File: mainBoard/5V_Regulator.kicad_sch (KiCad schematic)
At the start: 18 parts, among them IC1 LT8631IFE#PBF

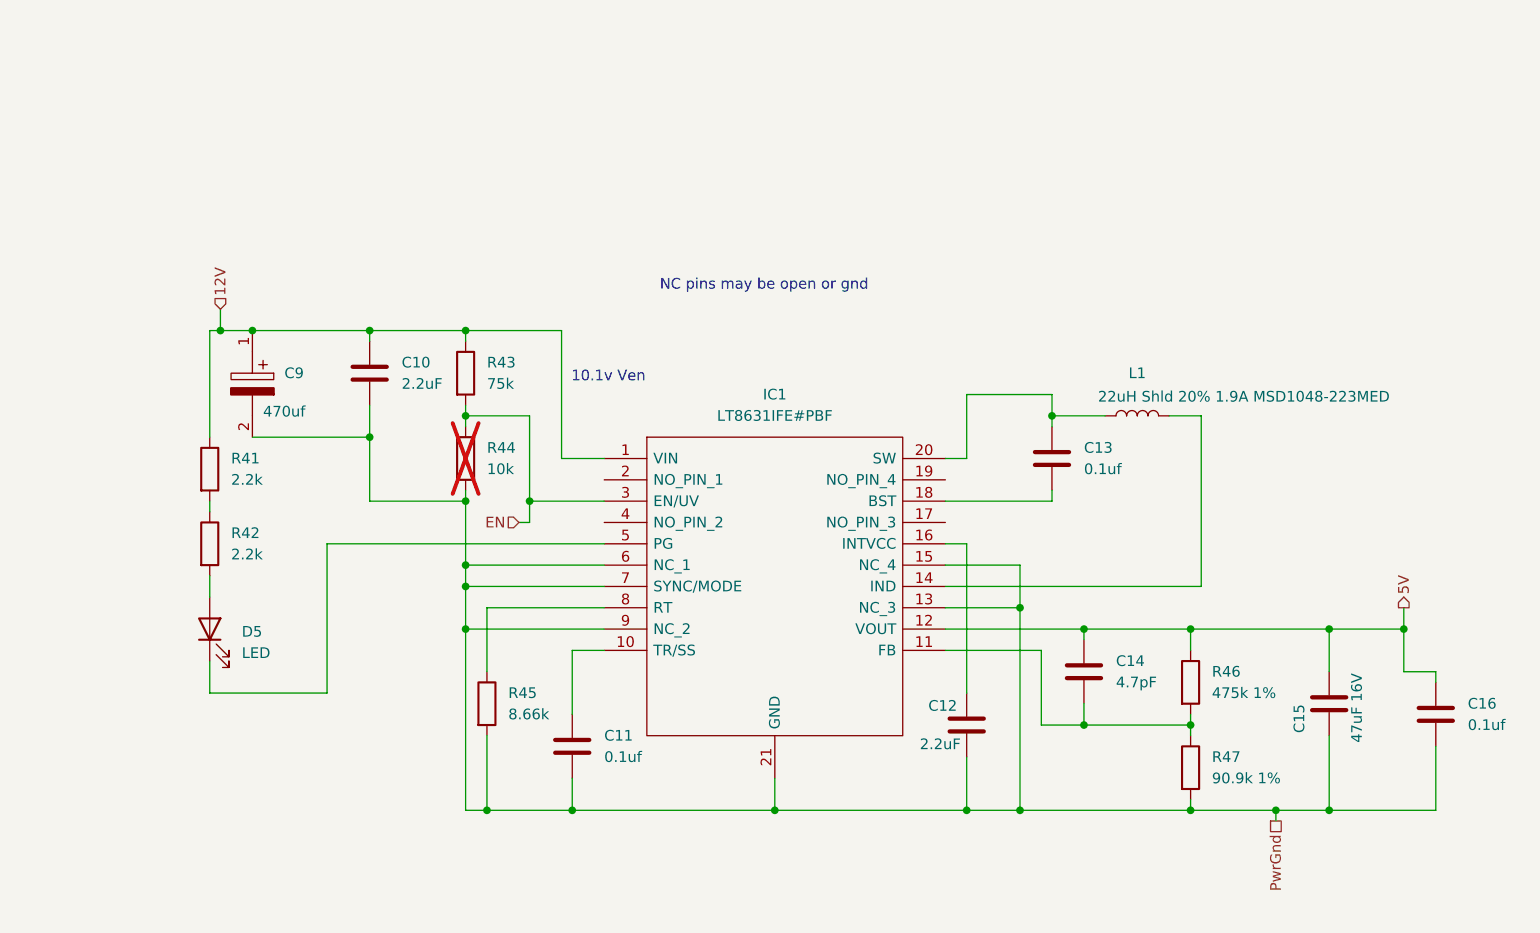
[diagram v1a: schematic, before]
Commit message: need to finish new regulators and run parts check on sch
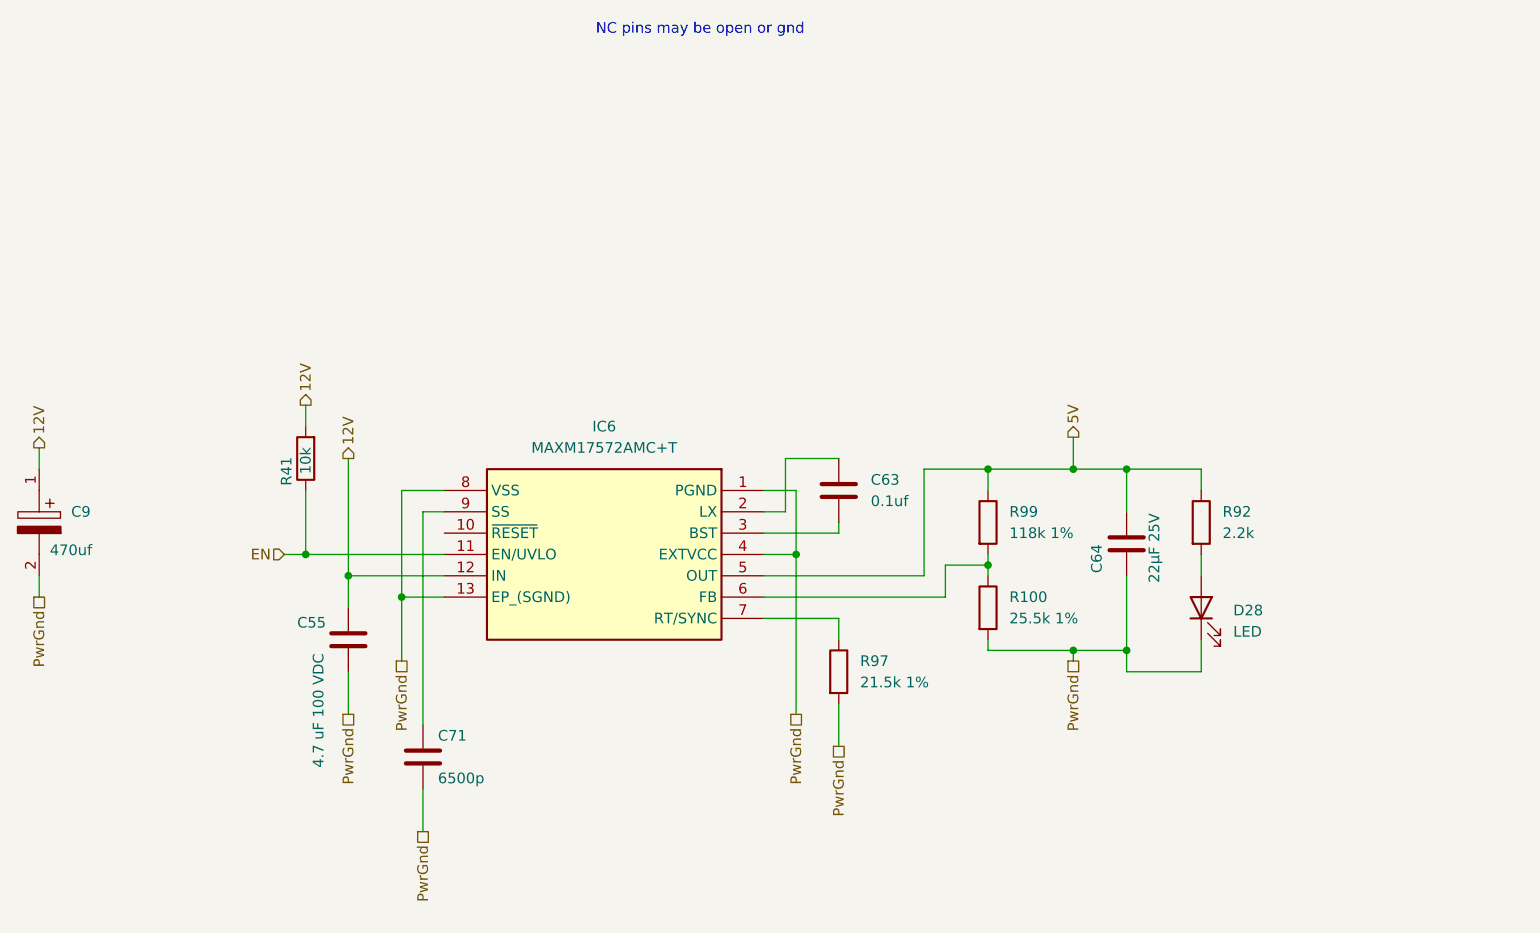
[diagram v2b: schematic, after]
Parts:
- removed C10, C12: 2.2uF, Capacitor_SMD:C_1206_3216Metric, symbol Device:C
- removed C11, C13, C16: 0.1uf, Capacitor_SMD:C_0402_1005Metric, symbol Device:C
- removed C14: 4.7pF, Capacitor_SMD:C_0402_1005Metric, symbol Device:C
- removed C15: 47uF 16V, Capacitor_SMD:C_1210_3225Metric, symbol Device:C
- removed D5: LED, LED_SMD:LED_0402_1005Metric, symbol Device:LED
- removed IC1: LT8631IFE#PBF, SamacSys_Parts:SOP65P640X120-21N, symbol SamacSys_Parts:LT8631IFE#PBF
- removed L1: 22uH Shld 20% 1.9A MSD1048-223MED, Inductor_SMD:L_Bourns_SRP1038C_10.0x10.0mm, symbol Device:L
- removed R42: 2.2k, Resistor_SMD:R_0805_2012Metric, symbol Device:R
- removed R43: 75k, Resistor_SMD:R_0402_1005Metric, symbol Device:R
- removed R44: 10k, Resistor_SMD:R_0402_1005Metric, symbol Device:R
- removed R45: 8.66k, Resistor_SMD:R_0402_1005Metric, symbol Device:R
- removed R46: 475k 1%, Resistor_SMD:R_0402_1005Metric, symbol Device:R
- removed R47: 90.9k 1%, Resistor_SMD:R_0402_1005Metric, symbol Device:R
- added C55: 4.7 uF 100 VDC, Capacitor_SMD:C_1206_3216Metric, symbol Device:C
- added C63: 0.1uf, Capacitor_SMD:C_0402_1005Metric, symbol Device:C
- added C64: 22μF 25V, Capacitor_SMD:C_1210_3225Metric, symbol Device:C
- added C71: 6500p, Capacitor_SMD:C_0402_1005Metric, symbol Device:C
- added D28: LED, LED_SMD:LED_0402_1005Metric, symbol Device:LED
- added IC6: MAXM17572AMC+T, parts:MAXM17572AMC, symbol MAXM17572AMC+T:MAXM17572AMC+T
- added R100: 25.5k 1%, Resistor_SMD:R_0402_1005Metric, symbol Device:R
- added R92: 2.2k, Resistor_SMD:R_0805_2012Metric, symbol Device:R
- added R97: 21.5k 1%, Resistor_SMD:R_0402_1005Metric, symbol Device:R
- added R99: 118k 1%, Resistor_SMD:R_0402_1005Metric, symbol Device:R
- R41: value 2.2k -> 10k; footprint Resistor_SMD:R_0805_2012Metric -> Resistor_SMD:R_0402_1005Metric
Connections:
- net 12V: now also R41.2, C55.1, IC6.12 (IN); no longer R41.1
- net 5V: now also C64.2, IC6.5 (OUT), R92.1, R99.1
- net EN: now also R41.1, IC6.11 (EN/UVLO)
- net PwrGnd: now also C55.2, C64.1, C71.2, D28.1 (K), IC6.1 (PGND), IC6.13 (EP_(SGND)), IC6.4 (EXTVCC), IC6.8 (VSS), R100.2, R97.2
- new net: IC6.6 (FB), R100.1, R99.2
- new net: C63.1, IC6.2 (LX)
- new net: C63.2, IC6.3 (BST)
- new net: IC6.7 (RT/SYNC), R97.1
- new net: C71.1, IC6.9 (SS)
- new net: D28.2 (A), R92.2
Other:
- note removed: "10.1v Ven"
- moved on the sheet: C9

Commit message: almost done
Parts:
- added C11: 2.2uF, Capacitor_SMD:C_1206_3216Metric, symbol Device:C
- C71: value 6500p -> 6800p
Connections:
- net PwrGnd: now also C11.2; no longer IC6.8 (VSS)
- new net: C11.1, IC6.8 (VCC)
- no-connect marks 0 -> 1
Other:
- moved on the sheet: C55, C71, R41

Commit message: i think the pcbs and sch are good
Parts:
- C71: Manufacturer_Name (none) -> Murata Electronics; Manufacturer_Part_Number (none) -> GRM1555C1H682GE01D; Mouser Part Number (none) -> https://www.mouser.com/en/ProductDetail/Murata-Electronics/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
- R100: Manufacturer_Part_Number (none) -> CRCW040225K5FKED
- R97: Manufacturer_Part_Number (none) -> CRCW040221K5FKED
- R99: Manufacturer_Part_Number (none) -> CRCW0402118KFKED
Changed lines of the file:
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@@
 			)
 		)
-		(property "Datasheet" "https://www.mouser.com/en/ProductDetail/Vishay/CRCW0402154KFKED?qs=sGAEpiMZZMtlubZbdhIBICyxlhGRQNJfRCzUCssnsug%3D"
+		(property "Datasheet" "https://www.mouser.com/en/ProductDetail/Vishay/CRCW040225K5FKED?qs=hD42E%2F8yzjq2MGDaErf%252BPQ%3D%3D"
+			(at 181.61 99.06 0)
+			(hide yes)
+			(show_name no)
+			(do_not_autoplace no)
+			(effects
+				(font
+					(size 1.27 1.27)
+				)
+			)
+		)
+		(property "Manufacturer_Part_Number" "CRCW040225K5FKED"
 			(at 181.61 99.06 0)
 			(hide yes)
@@
 			)
 		)
-		(property "Datasheet" "https://www.mouser.com/en/ProductDetail/Murata-Electronics/GCM155R71H104KE02J?qs=hNud%2FORuBR1wlwGPFWBVDg%3D%3D"
+		(property "Datasheet" "https://www.mouser.com/en/ProductDetail/Murata-Electronics/GRM1555C1H682GE01D?qs=d0WKAl%252BL4KZmZL9n8aRONA%3D%3D"
+			(at 113.03 116.84 0)
+			(hide yes)
+			(show_name no)
+			(do_not_autoplace no)
+			(effects
+				(font
+					(size 1.27 1.27)
+				)
+			)
+		)
+		(property "Mouser Part Number" "https://www.mouser.com/en/ProductDetail/Murata-Electronics/GRM1555C1H682GE01D?qs=d0WKAl%252BL4KZmZL9n8aRONA%3D%3D"
+			(at 113.03 116.84 0)
+			(hide yes)
+			(show_name no)
+			(do_not_autoplace no)
+			(effects
+				(font
+					(size 1.27 1.27)
+				)
+			)
+		)
+		(property "Manufacturer_Part_Number" "GRM1555C1H682GE01D"
+			(at 113.03 116.84 0)
+			(hide yes)
+			(show_name no)
+			(do_not_autoplace no)
+			(effects
+				(font
+					(size 1.27 1.27)
+				)
+			)
+		)
+		(property "Manufacturer_Name" "Murata Electronics"
 			(at 113.03 116.84 0)
 			(hide yes)
@@
 			)
 		)
-		(property "Datasheet" "https://www.mouser.com/ProductDetail/Vishay/CRCW04028K66FKEDC?qs=E3Y5ESvWgWPo4%2Fhc%252BAkQtg%3D%3D"
+		(property "Datasheet" "https://www.mouser.com/en/ProductDetail/Vishay/CRCW040221K5FKED?qs=oYI6rOI5zksElzYGuKPR%252BQ%3D%3D"
+			(at 163.83 106.68 0)
+			(hide yes)
+			(show_name no)
+			(do_not_autoplace no)
+			(effects
+				(font
+					(size 1.27 1.27)
+				)
+			)
+		)
+		(property "Manufacturer_Part_Number" "CRCW040221K5FKED"
 			(at 163.83 106.68 0)
 			(hide yes)
@@
 			)
 		)
-		(property "Datasheet" "https://www.mouser.com/ProductDetail/Vishay/CRCW0402422KFKED?qs=rzhQWu8UUS38CTZyFvhEkw%3D%3D"
+		(property "Datasheet" "https://www.mouser.com/en/ProductDetail/Vishay/CRCW0402118KFKED?qs=rlE3Te1NifzlSy4FZiG4wQ%3D%3D"
 			(at 181.61 88.9 0)
 			(hide yes)
+			(show_name no)
+			(do_not_autoplace no)
+			(effects
+				(font
+					(size 1.27 1.27)
+				)
+			)
+		)
+		(property "Manufacturer_Part_Number" "CRCW0402118KFKED"
+			(at 181.61 88.9 0)
+			(hide yes)
